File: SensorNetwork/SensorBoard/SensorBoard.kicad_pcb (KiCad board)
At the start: 2 copper layers, 23 x 23 mm, 14 parts, among them J2 CON_LEFT, J3 CON_RIGHT, U1 LTR-303ALS-01, U2 SHTC3, U4 MCP1700T-3302E_TT

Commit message: Documentions connections, local archive of 3d models, updates ibom
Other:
- board text added: "1"
- board text added: "GP0 INT_ALS GND I2C1SDA I2C1SCL I2C0SDA I2C0SCL GND"
- board text added: "RP2040"
- board text added: "VBUS VSYS GND 3V3EN 3V3_OUT VREF_Pico GP28 GND"
- board text added: "micro-USB"
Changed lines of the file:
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@@
     (pad "5" smd roundrect (at 0 0) (size 0.7 1.6) (layers "F.Cu" "F.Mask") (roundrect_rratio 0.25)
       (net 4 "unconnected-(U2-Pad5)") (pinfunction "NC") (pintype "no_connect"))
-    (model "/Users/neeraj/Dropbox/125_Systems/Kicad Libraries/3DModelsFreecad/SHT3C.wrl"
+    (model "${KIPRJMOD}/packages3D/SHT3C.wrl"
       (offset (xyz 0 0 0))
       (scale (xyz 1 1 1))
@@
     (pad "2" smd roundrect (at 0.95 0 180) (size 1 1.45) (layers "F.Cu" "F.Paste" "F.Mask") (roundrect_rratio 0.25)
       (net 2 "GND") (pintype "passive"))
-    (model "${KICAD6_3DMODEL_DIR}/Capacitor_SMD.3dshapes/C_0805_2012Metric.wrl"
+    (model "${KIPRJMOD}/packages3D/C_0805_2012Metric.wrl"
       (offset (xyz 0 0 0))
       (scale (xyz 1 1 1))
@@
     (pad "2" smd roundrect (at 0.825 0 90) (size 0.8 0.95) (layers "F.Cu" "F.Paste" "F.Mask") (roundrect_rratio 0.25)
       (net 15 "/INT_ALS") (pintype "passive"))
-    (model "${KICAD6_3DMODEL_DIR}/Resistor_SMD.3dshapes/R_0603_1608Metric.wrl"
+    (model "${KIPRJMOD}/packages3D/R_0603_1608Metric.wrl"
       (offset (xyz 0 0 0))
       (scale (xyz 1 1 1))
@@
     (pad "2" smd roundrect (at 0.825 0 180) (size 0.8 0.95) (layers "F.Cu" "F.Paste" "F.Mask") (roundrect_rratio 0.25)
       (net 13 "/I2C0_SDA") (pintype "passive"))
-    (model "${KICAD6_3DMODEL_DIR}/Resistor_SMD.3dshapes/R_0603_1608Metric.wrl"
+    (model "${KIPRJMOD}/packages3D/R_0603_1608Metric.wrl"
       (offset (xyz 0 0 0))
       (scale (xyz 1 1 1))
@@
     (pad "6" smd roundrect (at 0.9 -0.65 90) (size 0.65 0.3) (layers "F.Cu" "F.Paste" "F.Mask") (roundrect_rratio 0.25)
       (net 5 "/I2C1_SDA") (pinfunction "SDA") (pintype "bidirectional"))
-    (model "/Users/neeraj/Dropbox/125_Systems/Kicad Libraries/3DModelsFreecad/Cube.wrl"
+    (model "${KIPRJMOD}/packages3D/Cube.wrl"
       (offset (xyz -1 -1 0))
       (scale (xyz 1 1 1))
@@
     (pad "2" smd roundrect (at 0.825 0 180) (size 0.8 0.95) (layers "F.Cu" "F.Paste" "F.Mask") (roundrect_rratio 0.25)
       (net 14 "/I2C0_SCL") (pintype "passive"))
-    (model "${KICAD6_3DMODEL_DIR}/Resistor_SMD.3dshapes/R_0603_1608Metric.wrl"
+    (model "${KIPRJMOD}/packages3D/R_0603_1608Metric.wrl"
       (offset (xyz 0 0 0))
       (scale (xyz 1 1 1))
@@
     (pad "2" smd roundrect (at 0.95 0) (size 1 1.45) (layers "F.Cu" "F.Paste" "F.Mask") (roundrect_rratio 0.25)
       (net 2 "GND") (pintype "passive"))
-    (model "${KICAD6_3DMODEL_DIR}/Capacitor_SMD.3dshapes/C_0805_2012Metric.wrl"
+    (model "${KIPRJMOD}/packages3D/C_0805_2012Metric.wrl"
       (offset (xyz 0 0 0))
       (scale (xyz 1 1 1))
@@
     (pad "2" smd roundrect (at 0.95 0) (size 1 1.45) (layers "F.Cu" "F.Paste" "F.Mask") (roundrect_rratio 0.25)
       (net 2 "GND") (pintype "passive"))
-    (model "${KICAD6_3DMODEL_DIR}/Capacitor_SMD.3dshapes/C_0805_2012Metric.wrl"
+    (model "${KIPRJMOD}/packages3D/C_0805_2012Metric.wrl"
       (offset (xyz 0 0 0))
       (scale (xyz 1 1 1))
@@
     (pad "2" smd rect (at 1.65 0 90) (size 0.9 1.2) (layers "F.Cu" "F.Paste" "F.Mask")
       (net 6 "/VBUS") (pinfunction "A") (pintype "passive"))
-    (model "${KICAD6_3DMODEL_DIR}/Diode_SMD.3dshapes/D_SOD-123.wrl"
+    (model "${KIPRJMOD}/packages3D/D_SOD-123.wrl"
       (offset (xyz 0 0 0))
       (scale (xyz 1 1 1))
@@
     (pad "2" smd roundrect (at 0.95 0 270) (size 1 1.45) (layers "F.Cu" "F.Paste" "F.Mask") (roundrect_rratio 0.25)
       (net 2 "GND") (pintype "passive"))
-    (model "${KICAD6_3DMODEL_DIR}/Capacitor_SMD.3dshapes/C_0805_2012Metric.wrl"
+    (model "${KIPRJMOD}/packages3D/C_0805_2012Metric.wrl"
       (offset (xyz 0 0 0))
       (scale (xyz 1 1 1))
@@
     (pad "3" smd rect locked (at 1.05 0 90) (size 1.3 0.6) (layers "F.Cu" "F.Paste" "F.Mask")
       (net 3 "Net-(C2-Pad1)") (pinfunction "IN") (pintype "power_in") (solder_mask_margin 0.07))
-    (model "${KICAD6_3DMODEL_DIR}/Package_TO_SOT_SMD.3dshapes/SOT-23.step"
+    (model "${KIPRJMOD}/packages3D/SOT-23.step"
       (offset (xyz 0 0 0))
       (scale (xyz 1 1 1))
@@
     (pad "2" smd rect (at 1.75 0 180) (size 1.3 1.7) (layers "F.Cu" "F.Paste" "F.Mask")
       (net 2 "GND") (pinfunction "A") (pintype "passive"))
-    (model "${KICAD6_3DMODEL_DIR}/Diode_SMD.3dshapes/D_MiniMELF.wrl"
+    (model "${KIPRJMOD}/packages3D/D_MiniMELF.wrl"
       (offset (xyz 0 0 0))
       (scale (xyz 1 1 1))
@@
     (pad "8" thru_hole oval locked (at 0 -17.78 180) (size 1.7 1.7) (drill 1) (layers *.Cu *.Mask)
       (net 2 "GND") (pinfunction "Pin_8") (pintype "passive"))
-    (model "${KICAD6_3DMODEL_DIR}/Connector_PinHeader_2.54mm.3dshapes/PinHeader_1x08_P2.54mm_Vertical.wrl"
+    (model "${KIPRJMOD}/packages3D/PinHeader_1x08_P2.54mm_Vertical.wrl"
       (offset (xyz 0 0 0))
       (scale (xyz 1 1 1))
@@
     (pad "8" thru_hole oval locked (at 0 -17.78 180) (size 1.7 1.7) (drill 1) (layers *.Cu *.Mask)
       (net 2 "GND") (pinfunction "Pin_8") (pintype "passive"))
-    (model "${KICAD6_3DMODEL_DIR}/Connector_PinHeader_2.54mm.3dshapes/PinHeader_1x08_P2.54mm_Vertical.wrl"
+    (model "${KIPRJMOD}/packages3D/PinHeader_1x08_P2.54mm_Vertical.wrl"
       (offset (xyz 0 0 0))
       (scale (xyz 1 1 1))
@@
   (gr_line (start 70.5 47.5) (end 70.5 70.5) (layer "Edge.Cuts") (width 0.1))
   (gr_line (start 70.5 70.5) (end 47.5 70.5) (layer "Edge.Cuts") (width 0.1))
+  (gr_rect (start 54.7 43.95) (end 63.7 48) (layer "User.1") (width 0.15) (fill none))
+  (gr_rect (start 54 70.95) (end 64.3 80.1) (layer "User.1") (width 0.15) (fill none))
   (gr_text "125 Systems\nTHSensorBoard\nRev 1" (at 56.5 50.5) (layer "F.SilkS")
     (effects (font (size 0.8 0.8) (thickness 0.2)))
   )
+  (gr_text "RP2040" (at 59 75.2) (layer "User.1")
+    (effects (font (size 1 1) (thickness 0.15)))
+  )
+  (gr_text "1" (at 49.95 45.85) (layer "User.1")
+    (effects (font (size 3 3) (thickness 0.15)))
+  )
+  (gr_text "1" (at 68.2 45.85) (layer "User.1")
+    (effects (font (size 3 3) (thickness 0.15)))
+  )
+  (gr_text "VBUS\nVSYS\nGND\n3V3EN\n3V3_OUT\nVREF_Pico\nGP28\nGND" (at 70.5 59.3) (layer "User.1")
+    (effects (font (size 1.6 1.6) (thickness 0.15)) (justify left))
+  )
+  (gr_text "micro-USB" (at 58.4 42.3) (layer "User.1")
+    (effects (font (size 1 1) (thickness 0.15)))
+  )
+  (gr_text "GP0\nINT_ALS\nGND\nI2C1SDA\nI2C1SCL\nI2C0SDA\nI2C0SCL\nGND" (at 47.4 59) (layer "User.1")
+    (effects (font (size 1.6 1.6) (thickness 0.15)) (justify right))
+  )
   (via (at 57.76 67.44) (size 0.5) (drill 0.3) (layers "F.Cu" "B.Cu") (free) (net 0))

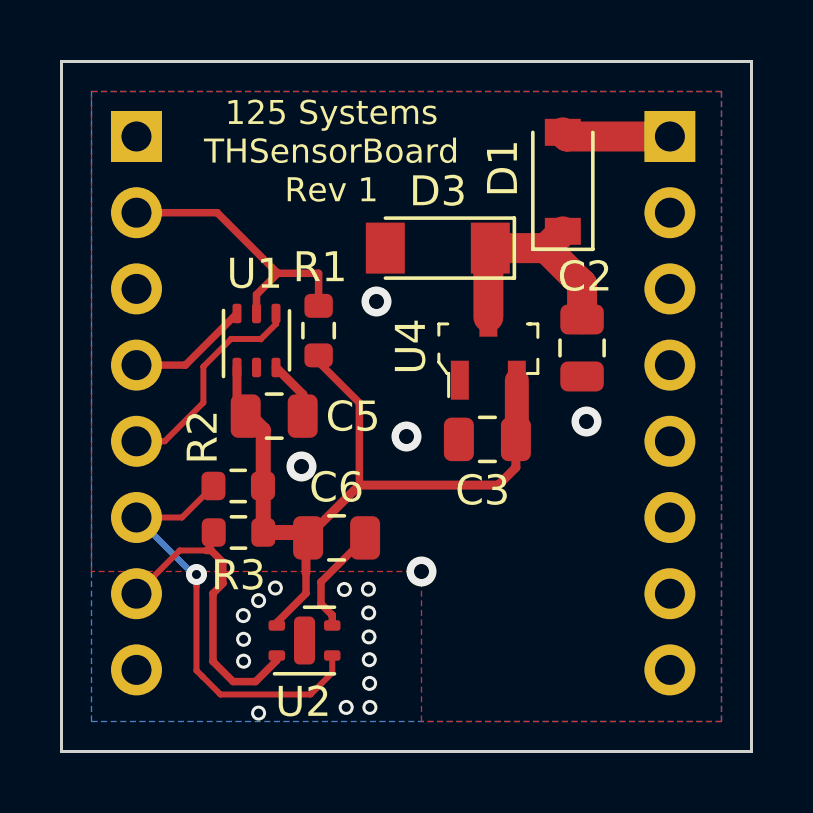
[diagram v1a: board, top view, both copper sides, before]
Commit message: Fixes schematic and PCB, update corresponding figures
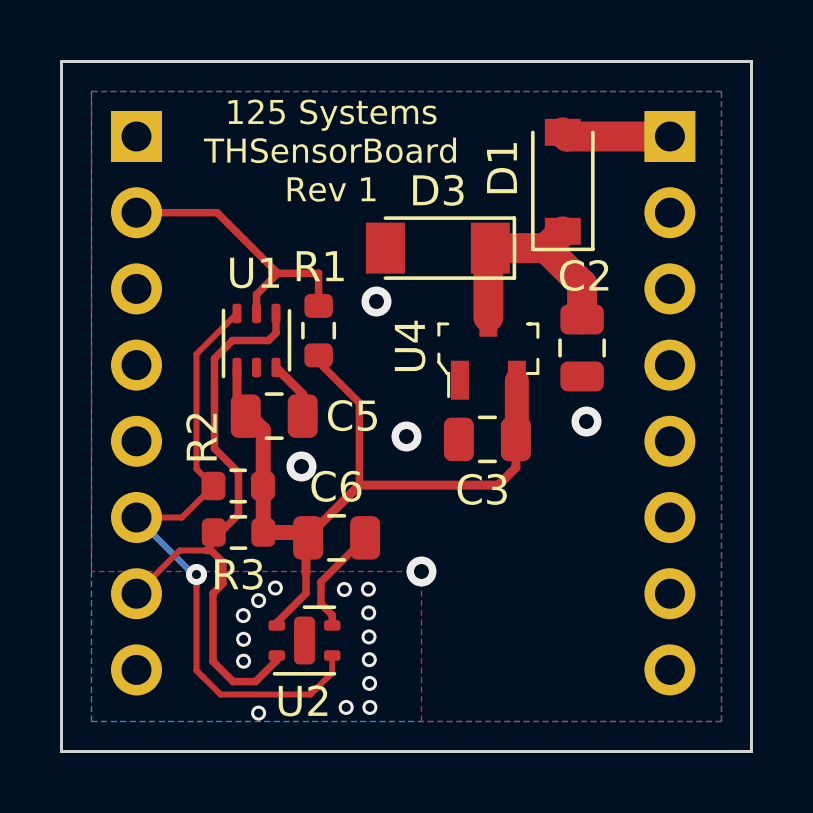
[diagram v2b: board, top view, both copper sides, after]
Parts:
- R2, R3: value 5k1 -> 10k
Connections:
- U1 pad 4: /I2C1_SCL -> /I2C0_SCL
- U1 pad 6: /I2C1_SDA -> /I2C0_SDA
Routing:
- net /I2C0_SCL: track 10.3 -> 20.0 mm
- net /I2C1_SCL: track 7.33 -> 0.00 mm
- net /I2C0_SDA: track 14.7 -> 21.3 mm
- net /I2C1_SDA: track 4.06 -> 0.00 mm
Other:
- board text added: "GP0 INT_ALS GND NC NC I2C0SDA I2C0SCL GND"
- board text removed: "GP0 INT_ALS GND I2C1SDA I2C1SCL I2C0SDA I2C0SCL GND"
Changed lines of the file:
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@@
       (effects (font (size 1 1) (thickness 0.15)))
     )
-    (fp_text value "5k1" (at 0 1.43 180) (layer "F.Fab")
+    (fp_text value "10k" (at 0 1.43 180) (layer "F.Fab")
       (effects (font (size 1 1) (thickness 0.15)))
     )
@@
       (net 2 "GND") (pinfunction "GND") (pintype "power_in"))
     (pad "4" smd roundrect (at 0.9 0.65 90) (size 0.65 0.3) (layers "F.Cu" "F.Paste" "F.Mask") (roundrect_rratio 0.25)
-      (net 12 "/I2C1_SCL") (pinfunction "SCL") (pintype "input"))
+      (net 14 "/I2C0_SCL") (pinfunction "SCL") (pintype "input"))
     (pad "5" smd roundrect (at 0.9 0 90) (size 0.65 0.3) (layers "F.Cu" "F.Paste" "F.Mask") (roundrect_rratio 0.25)
       (net 15 "/INT_ALS") (pinfunction "INT") (pintype "open_collector"))
     (pad "6" smd roundrect (at 0.9 -0.65 90) (size 0.65 0.3) (layers "F.Cu" "F.Paste" "F.Mask") (roundrect_rratio 0.25)
-      (net 5 "/I2C1_SDA") (pinfunction "SDA") (pintype "bidirectional"))
+      (net 13 "/I2C0_SDA") (pinfunction "SDA") (pintype "bidirectional"))
     (model "${KIPRJMOD}/packages3D/Cube.wrl"
       (offset (xyz -1 -1 0))
@@
       (effects (font (size 1 1) (thickness 0.15)))
     )
-    (fp_text value "5k1" (at 0 1.43 180) (layer "F.Fab")
+    (fp_text value "10k" (at 0 1.43 180) (layer "F.Fab")
       (effects (font (size 1 1) (thickness 0.15)))
     )
@@
     (effects (font (size 1 1) (thickness 0.15)))
   )
-  (gr_text "GP0\nINT_ALS\nGND\nI2C1SDA\nI2C1SCL\nI2C0SDA\nI2C0SCL\nGND" (at 47.4 59) (layer "User.1")
+  (gr_text "GP0\nINT_ALS\nGND\nNC\nNC\nI2C0SDA\nI2C0SCL\nGND" (at 47.4 59) (layer "User.1")
     (effects (font (size 1.6 1.6) (thickness 0.15)) (justify right))
   )
@@
   (segment (start 64.8528 56.0984) (end 64.8528 54.9224) (width 1) (layer "F.Cu") (net 3))
   (segment (start 61.7956 53.721) (end 63.6514 53.721) (width 1) (layer "F.Cu") (net 3))
-  (segment (start 50 57.62) (end 51.63 57.62) (width 0.25) (layer "F.Cu") (net 5))
-  (segment (start 51.63 57.62) (end 53.35 55.9) (width 0.25) (layer "F.Cu") (net 5))
   (segment (start 64.35 50) (end 64.2112 49.8612) (width 1) (layer "F.Cu") (net 6))
   (segment (start 67.78 50) (end 64.35 50) (width 1) (layer "F.Cu") (net 6))
-  (segment (start 50 60.16) (end 50.94 60.16) (width 0.2) (layer "F.Cu") (net 12))
-  (segment (start 52.23 57.67) (end 53.15 56.75) (width 0.2) (layer "F.Cu") (net 12))
-  (segment (start 53.15 56.75) (end 54.13 56.75) (width 0.2) (layer "F.Cu") (net 12))
-  (segment (start 52.23 58.87) (end 52.23 57.67) (width 0.2) (layer "F.Cu") (net 12))
-  (segment (start 54.14 56.76) (end 54.65 56.25) (width 0.2) (layer "F.Cu") (net 12))
-  (segment (start 50.94 60.16) (end 52.23 58.87) (width 0.2) (layer "F.Cu") (net 12))
-  (segment (start 54.65 56.25) (end 54.65 55.9) (width 0.2) (layer "F.Cu") (net 12))
-  (segment (start 54.13 56.75) (end 54.14 56.76) (width 0.2) (layer "F.Cu") (net 12))
   (segment (start 56.525 67.3) (end 56.525 67.875) (width 0.2) (layer "F.Cu") (net 13))
   (segment (start 52 65) (end 52 64.6) (width 0.2) (layer "F.Cu") (net 13))
   (segment (start 52.8 68.6) (end 52.2 68) (width 0.2) (layer "F.Cu") (net 13))
+  (segment (start 52 57.25) (end 53.35 55.9) (width 0.2) (layer "F.Cu") (net 13))
   (segment (start 52.2 68) (end 52 67.8) (width 0.2) (layer "F.Cu") (net 13))
   (segment (start 50 62.7) (end 51.515 62.7) (width 0.2) (layer "F.Cu") (net 13))
   (segment (start 56.525 67.875) (end 55.8 68.6) (width 0.2) (layer "F.Cu") (net 13))
   (segment (start 55.8 68.6) (end 52.8 68.6) (width 0.2) (layer "F.Cu") (net 13))
+  (segment (start 52 61.085) (end 52 57.25) (width 0.2) (layer "F.Cu") (net 13))
+  (segment (start 52.565 61.65) (end 52 61.085) (width 0.2) (layer "F.Cu") (net 13))
   (segment (start 52 67.8) (end 52 65) (width 0.2) (layer "F.Cu") (net 13))
   (segment (start 51.515 62.7) (end 52.565 61.65) (width 0.2) (layer "F.Cu") (net 13))
@@
   (segment (start 51.9 64.6) (end 50 62.7) (width 0.2) (layer "B.Cu") (net 13))
   (segment (start 52 64.6) (end 51.9 64.6) (width 0.2) (layer "B.Cu") (net 13))
+  (segment (start 52.6 60.4) (end 53.4 61.2) (width 0.25) (layer "F.Cu") (net 14))
+  (segment (start 53.4 62.6) (end 52.8 63.2) (width 0.25) (layer "F.Cu") (net 14))
   (segment (start 52.49 63.8) (end 52.319239 63.8) (width 0.25) (layer "F.Cu") (net 14))
   (segment (start 52.55 67.5) (end 52.55 65.23) (width 0.25) (layer "F.Cu") (net 14))
   (segment (start 54.675 67.3) (end 54.675 67.465) (width 0.25) (layer "F.Cu") (net 14))
+  (segment (start 53.4 61.2) (end 53.4 62.6) (width 0.25) (layer "F.Cu") (net 14))
+  (segment (start 52.8 63.2) (end 52.575 63.2) (width 0.25) (layer "F.Cu") (net 14))
+  (segment (start 53.2 56.8) (end 52.6 57.4) (width 0.25) (layer "F.Cu") (net 14))
   (segment (start 52.319239 63.8) (end 51.44 63.8) (width 0.2) (layer "F.Cu") (net 14))
   (segment (start 52.55 65.23) (end 52.88 64.9) (width 0.25) (layer "F.Cu") (net 14))
+  (segment (start 54.65 56.55) (end 54.4 56.8) (width 0.25) (layer "F.Cu") (net 14))
+  (segment (start 52.6 57.4) (end 52.6 60.4) (width 0.25) (layer "F.Cu") (net 14))
   (segment (start 54.675 67.465) (end 53.97 68.17) (width 0.25) (layer "F.Cu") (net 14))
   (segment (start 53.22 68.17) (end 52.55 67.5) (width 0.25) (layer "F.Cu") (net 14))
   (segment (start 51.44 63.8) (end 50 65.24) (width 0.2) (layer "F.Cu") (net 14))
   (segment (start 52.88 64.9) (end 52.88 64.19) (width 0.25) (layer "F.Cu") (net 14))
+  (segment (start 54.65 55.9) (end 54.65 56.55) (width 0.25) (layer "F.Cu") (net 14))
   (segment (start 52.88 64.19) (end 52.49 63.8) (width 0.25) (layer "F.Cu") (net 14))
   (segment (start 53.97 68.17) (end 53.22 68.17) (width 0.25) (layer "F.Cu") (net 14))
+  (segment (start 54.4 56.8) (end 53.2 56.8) (width 0.25) (layer "F.Cu") (net 14))
   (segment (start 52.6025 63.516739) (end 52.319239 63.8) (width 0.2) (layer "F.Cu") (net 14))
   (segment (start 52.69 52.54) (end 50 52.54) (width 0.25) (layer "F.Cu") (net 15))
